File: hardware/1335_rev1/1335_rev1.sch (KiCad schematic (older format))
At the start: 12 parts, among them J1 Screw_Terminal_01x05, J2 Screw_Terminal_01x05, U1 A1335

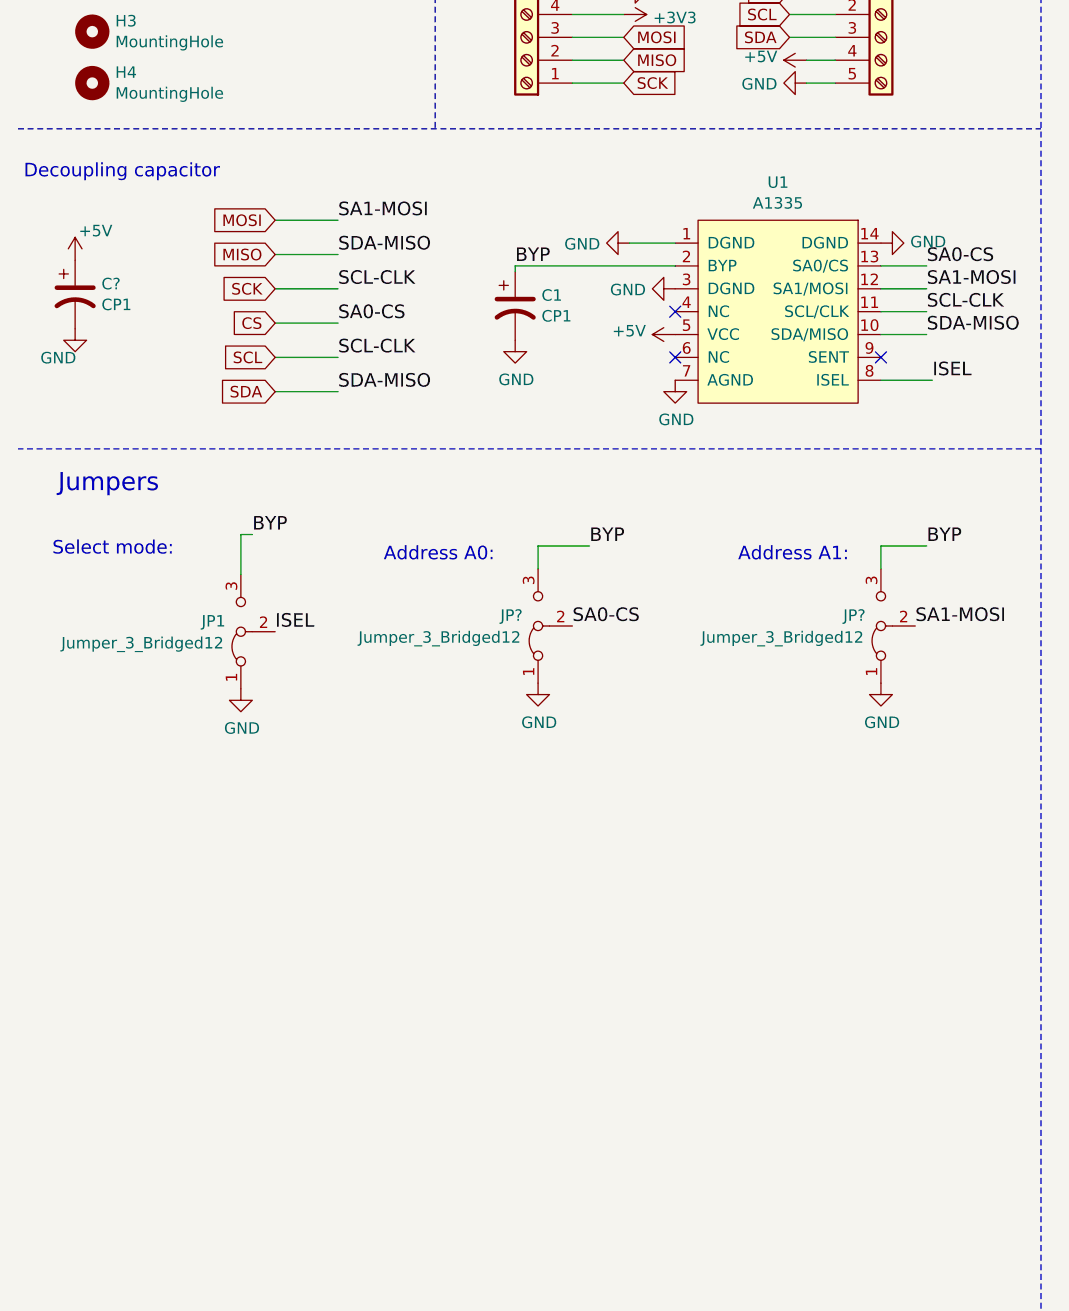
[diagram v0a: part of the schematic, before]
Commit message: Add 3d models, send to review pcb
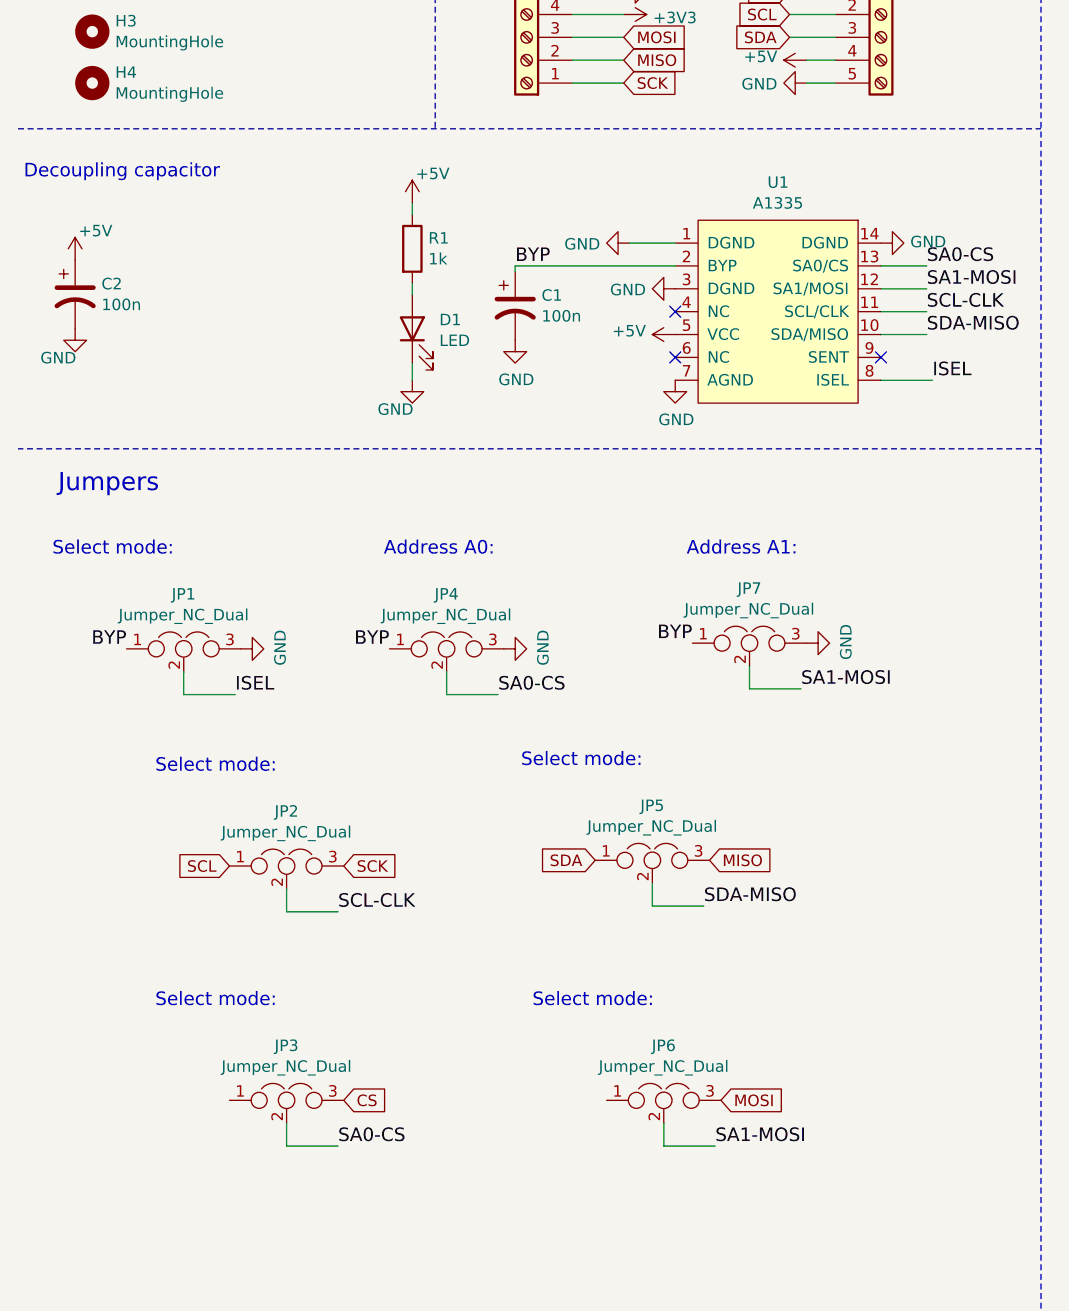
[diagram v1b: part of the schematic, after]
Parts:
- removed JP1, JP? (x2): Jumper_3_Bridged12, Jumper:SolderJumper-3_P1.3mm_Bridged2Bar12_Pad1.0x1.5mm, symbol Jumper:Jumper_3_Bridged12
- added D1: LED, LED_SMD:LED_0603_1608Metric, symbol Device:LED
- added JP1, JP2, JP3, JP4, JP5, JP6, JP7: Jumper_NC_Dual, Jumper:SolderJumper-3_P1.3mm_Open_RoundedPad1.0x1.5mm_NumberLabels, symbol Device:Jumper_NC_Dual
- added R1: 1k, Resistor_SMD:R_0603_1608Metric, symbol Device:R
- C1: value CP1 -> 100n
- C2: renamed from C?; value CP1 -> 100n
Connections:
- net +5V: now also R1.1
- net BYP: now also JP1.1, JP4.1, JP7.1
- net CS: now also JP3.3; no longer U1.13 (SA0/CS)
- net GND: now also D1.1 (K), JP1.3, JP4.3, JP7.3
- net ISEL: now also JP1.2
- net MISO: now also JP5.3; no longer J2.3 (Pin_3), U1.10 (SDA/MISO)
- net MOSI: now also JP6.3; no longer U1.12 (SA1/MOSI)
- net SCK: now also JP2.3; no longer J2.2 (Pin_2), U1.11 (SCL/CLK)
- new net: D1.2 (A), R1.2
- new net SA0-CS: JP3.2, JP4.2, U1.13 (SA0/CS)
- new net SA1-MOSI: JP6.2, JP7.2, U1.12 (SA1/MOSI)
- new net SCL: J2.2 (Pin_2), JP2.1
- new net SCL-CLK: JP2.2, U1.11 (SCL/CLK)
- new net SDA: J2.3 (Pin_3), JP5.1
- new net SDA-MISO: JP5.2, U1.10 (SDA/MISO)

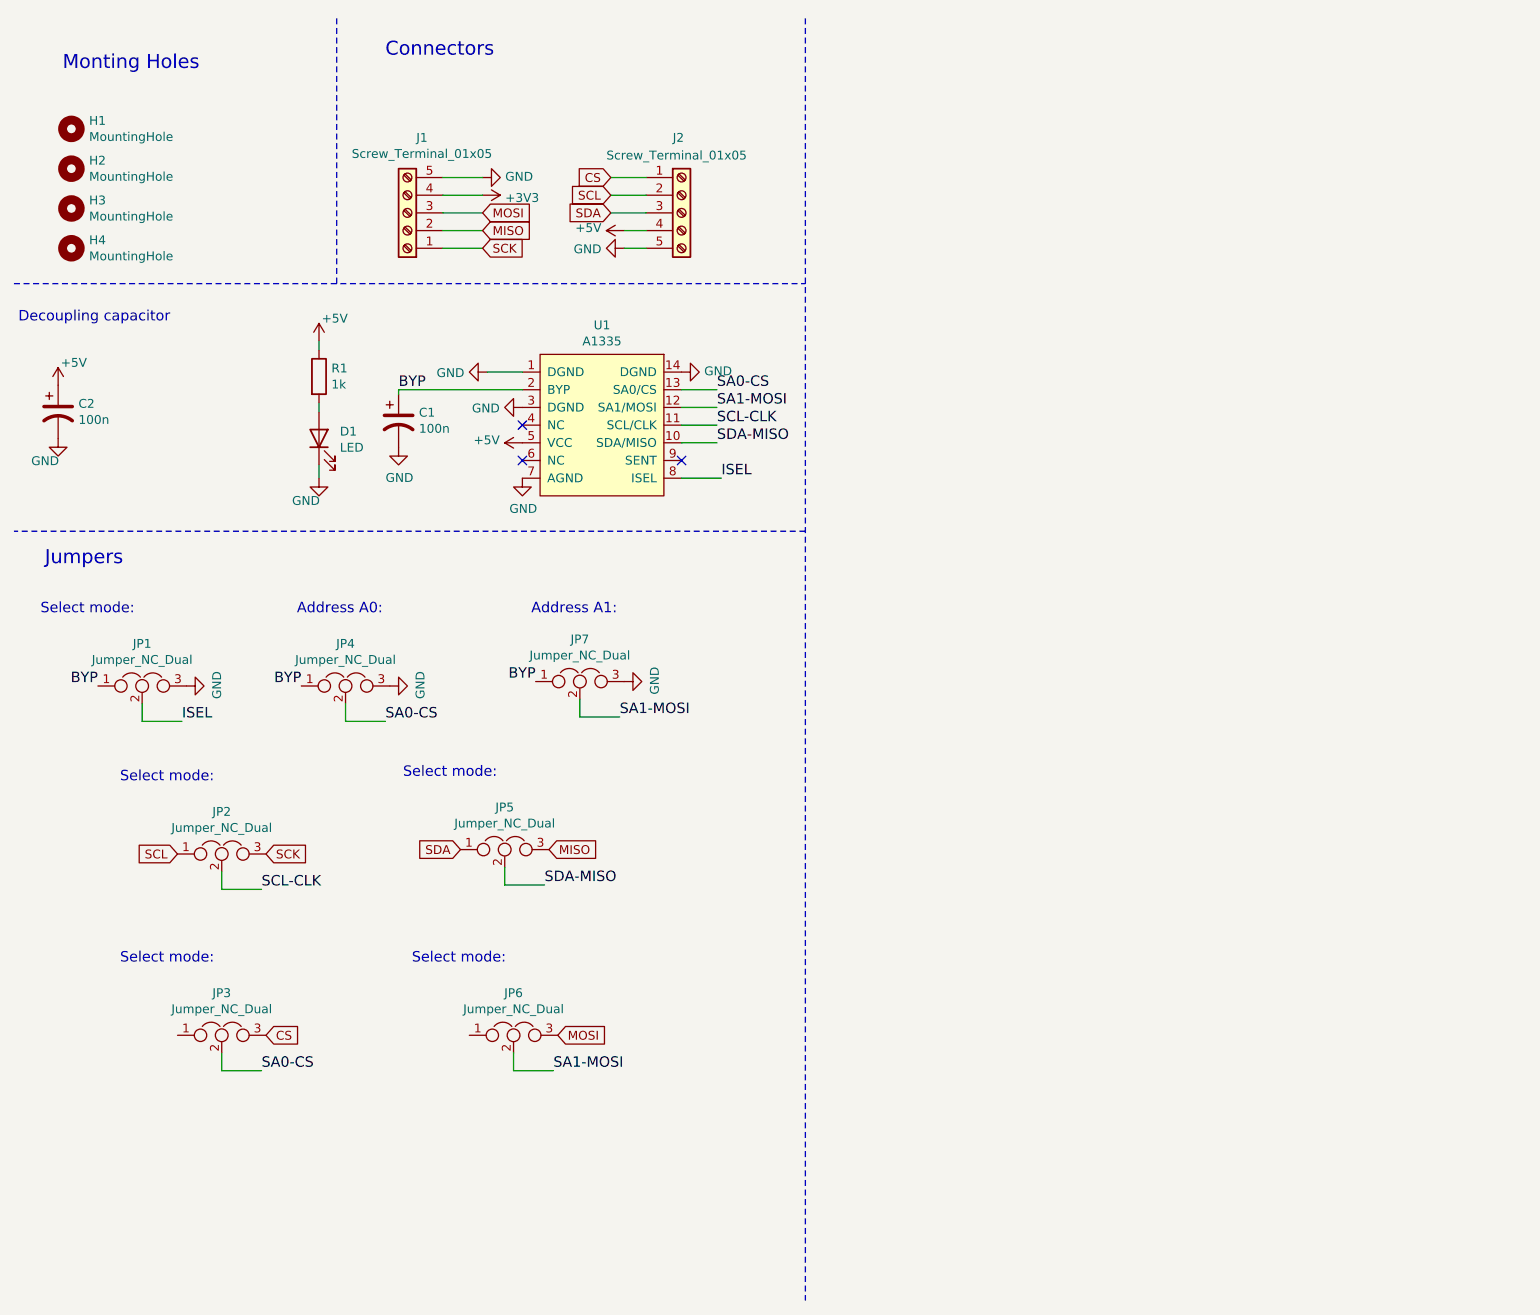
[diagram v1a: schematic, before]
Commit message: Add connectors and pull up resistors
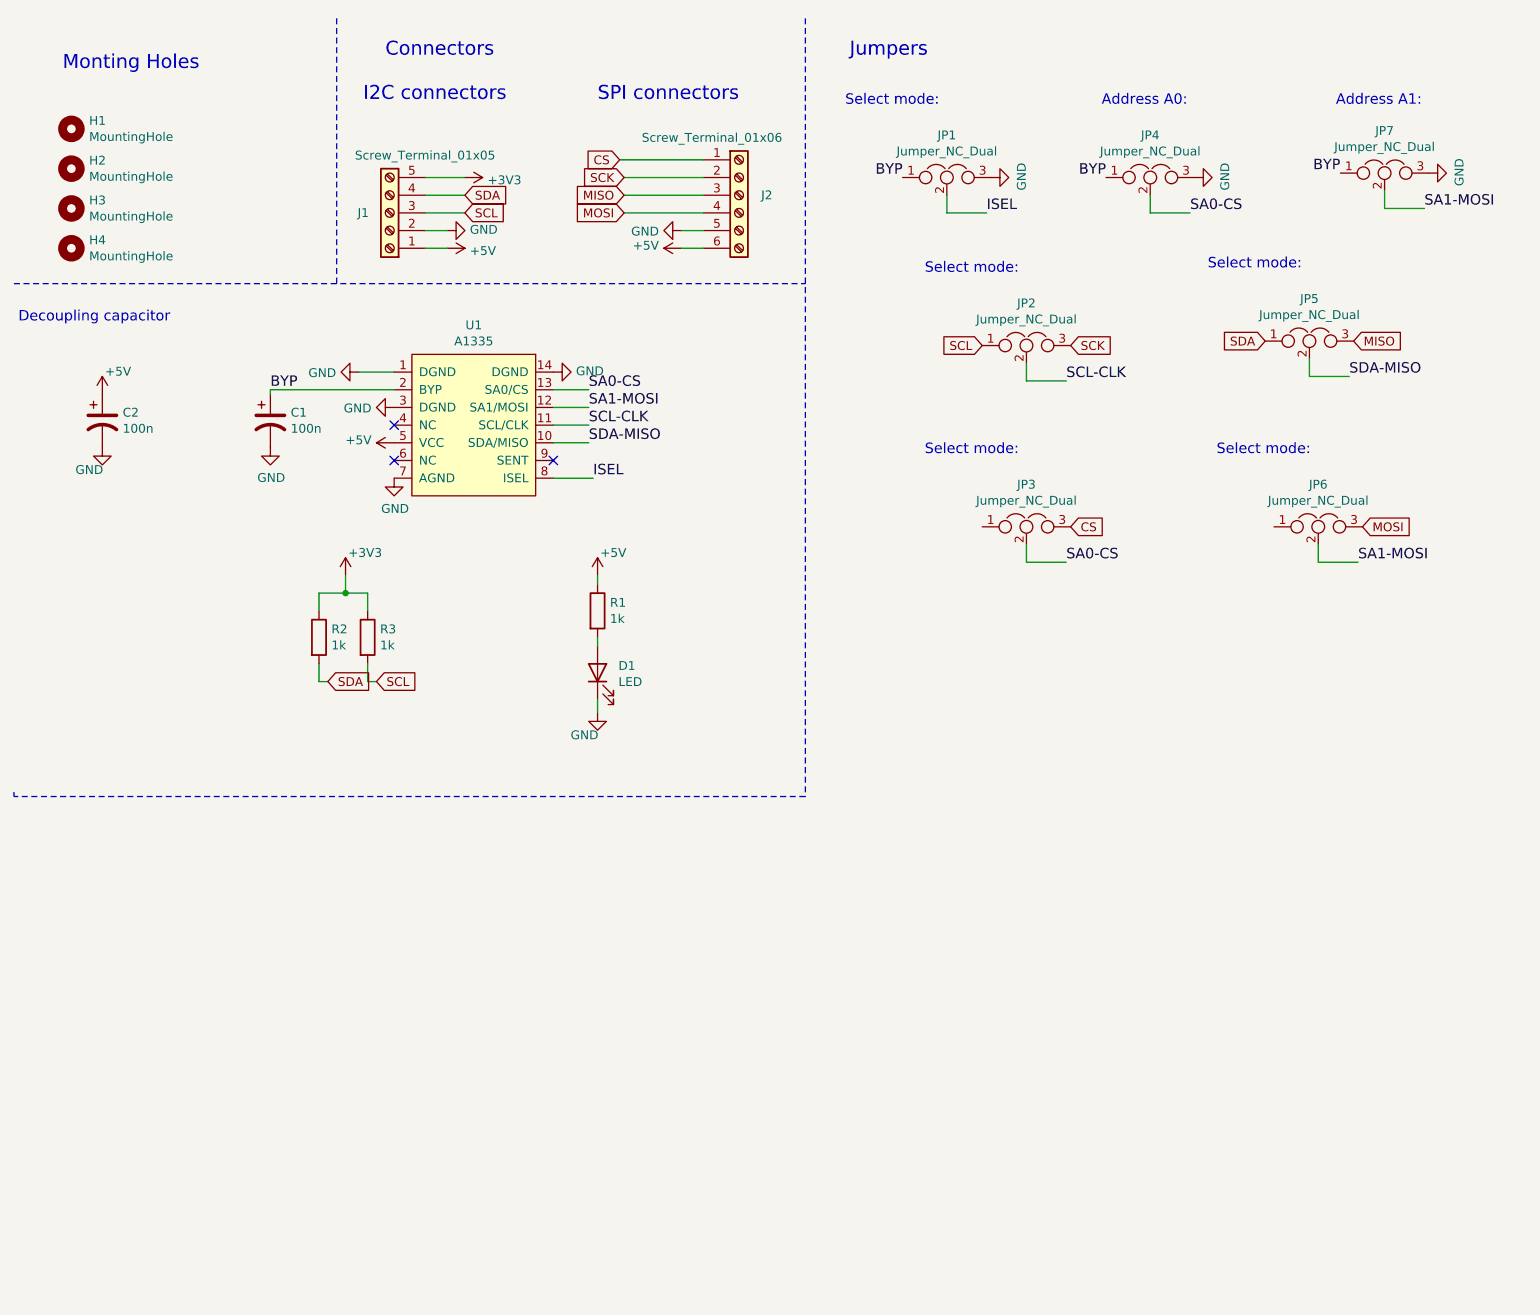
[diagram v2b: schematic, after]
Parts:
- removed J2: Screw_Terminal_01x05, Terminal_Block_WR_TBL:terminal_block_1x05_45DEG_3.81MM_5POS, symbol Connector:Screw_Terminal_01x05
- added J2: Screw_Terminal_01x06, Connector_PinHeader_2.54mm:PinHeader_1x06_P2.54mm_Horizontal, symbol Connector:Screw_Terminal_01x06
- added R2, R3: 1k, Resistor_SMD:R_0603_1608Metric, symbol Device:R
- J1: footprint Terminal_Block_WR_TBL:terminal_block_1x05_45DEG_3.81MM_5POS -> Connector_PinHeader_2.54mm:PinHeader_1x05_P2.54mm_Horizontal
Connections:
- net +3V3: now also J1.5 (Pin_5), R2.1, R3.1; no longer J1.4 (Pin_4)
- net +5V: now also J1.1 (Pin_1), J2.6 (Pin_6)
- net CS: now also J2.1 (Pin_1)
- net GND: now also J1.2 (Pin_2), J2.5 (Pin_5); no longer J1.5 (Pin_5)
- net MISO: now also J2.3 (Pin_3); no longer J1.2 (Pin_2)
- net MOSI: now also J2.4 (Pin_4); no longer J1.3 (Pin_3)
- net SCK: now also J2.2 (Pin_2); no longer J1.1 (Pin_1)
- net SCL: now also J1.3 (Pin_3), R3.2
- net SDA: now also J1.4 (Pin_4), R2.2
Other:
- note added: "I2C connectors"
- note added: "SPI connectors"
- moved on the sheet: C1, C2, D1, JP1, JP2, JP3, JP4, JP5, JP6, JP7, R1, U1

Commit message: Add F.sliks anotations
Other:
- note added: "1-2 SPI Mode\n2-3 I2C Mode"
- note added: "1-2\n2-3"
- moved on the sheet: JP2, JP3, JP5, JP6
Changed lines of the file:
@@
 Text Label 8500 1575 0    59   ~ 0
 SA1-MOSI
-Text Notes 5675 1950 0    59   ~ 0
+Text Notes 5650 2325 0    59   ~ 0
 Select mode:\n
 $Comp
 L Device:Jumper_NC_Dual JP2
 U 1 1 604B71D7
-P 6250 2350
-F 0 "JP2" H 6250 2589 50  0000 C CNN
-F 1 "Jumper_NC_Dual" H 6250 2498 50  0000 C CNN
-F 2 "Jumper:SolderJumper-3_P1.3mm_Open_RoundedPad1.0x1.5mm_NumberLabels" H 6250 2350 50  0001 C CNN
-F 3 "~" H 6250 2350 50  0001 C CNN
-	1    6250 2350
-	1    0    0    -1
-$EndComp
-Wire Wire Line
-	6250 2450 6250 2550
-Wire Wire Line
-	6250 2550 6475 2550
-Text Notes 7275 1925 0    59   ~ 0
+P 6225 2725
+F 0 "JP2" H 6225 2964 50  0000 C CNN
+F 1 "Jumper_NC_Dual" H 6225 2873 50  0000 C CNN
+F 2 "Jumper:SolderJumper-3_P1.3mm_Open_RoundedPad1.0x1.5mm_NumberLabels" H 6225 2725 50  0001 C CNN
+F 3 "~" H 6225 2725 50  0001 C CNN
+	1    6225 2725
+	1    0    0    -1
+$EndComp
+Wire Wire Line
+	6225 2825 6225 2925
+Wire Wire Line
+	6225 2925 6450 2925
+Text Notes 7250 2300 0    59   ~ 0
 Select mode:\n
 $Comp
 L Device:Jumper_NC_Dual JP5
 U 1 1 604B9F66
-P 7850 2325
-F 0 "JP5" H 7850 2564 50  0000 C CNN
-F 1 "Jumper_NC_Dual" H 7850 2473 50  0000 C CNN
-F 2 "Jumper:SolderJumper-3_P1.3mm_Open_RoundedPad1.0x1.5mm_NumberLabels" H 7850 2325 50  0001 C CNN
-F 3 "~" H 7850 2325 50  0001 C CNN
-	1    7850 2325
-	1    0    0    -1
-$EndComp
-Wire Wire Line
-	7850 2425 7850 2525
-Wire Wire Line
-	7850 2525 8075 2525
-Text Notes 5675 2975 0    59   ~ 0
+P 7825 2700
+F 0 "JP5" H 7825 2939 50  0000 C CNN
+F 1 "Jumper_NC_Dual" H 7825 2848 50  0000 C CNN
+F 2 "Jumper:SolderJumper-3_P1.3mm_Open_RoundedPad1.0x1.5mm_NumberLabels" H 7825 2700 50  0001 C CNN
+F 3 "~" H 7825 2700 50  0001 C CNN
+	1    7825 2700
+	1    0    0    -1
+$EndComp
+Wire Wire Line
+	7825 2800 7825 2900
+Wire Wire Line
+	7825 2900 8050 2900
+Text Notes 5650 3350 0    59   ~ 0
 Select mode:\n
 $Comp
 L Device:Jumper_NC_Dual JP3
 U 1 1 604BBF53
-P 6250 3375
-F 0 "JP3" H 6250 3614 50  0000 C CNN
-F 1 "Jumper_NC_Dual" H 6250 3523 50  0000 C CNN
-F 2 "Jumper:SolderJumper-3_P1.3mm_Open_RoundedPad1.0x1.5mm_NumberLabels" H 6250 3375 50  0001 C CNN
-F 3 "~" H 6250 3375 50  0001 C CNN
-	1    6250 3375
-	1    0    0    -1
-$EndComp
-Wire Wire Line
-	6250 3475 6250 3575
-Wire Wire Line
-	6250 3575 6475 3575
-Text Notes 7325 2975 0    59   ~ 0
+P 6225 3750
+F 0 "JP3" H 6225 3989 50  0000 C CNN
+F 1 "Jumper_NC_Dual" H 6225 3898 50  0000 C CNN
+F 2 "Jumper:SolderJumper-3_P1.3mm_Open_RoundedPad1.0x1.5mm_NumberLabels" H 6225 3750 50  0001 C CNN
+F 3 "~" H 6225 3750 50  0001 C CNN
+	1    6225 3750
+	1    0    0    -1
+$EndComp
+Wire Wire Line
+	6225 3850 6225 3950
+Wire Wire Line
+	6225 3950 6450 3950
+Text Notes 7300 3350 0    59   ~ 0
 Select mode:\n
 $Comp
 L Device:Jumper_NC_Dual JP6
 U 1 1 604BD230
-P 7900 3375
-F 0 "JP6" H 7900 3614 50  0000 C CNN
-F 1 "Jumper_NC_Dual" H 7900 3523 50  0000 C CNN
-F 2 "Jumper:SolderJumper-3_P1.3mm_Open_RoundedPad1.0x1.5mm_NumberLabels" H 7900 3375 50  0001 C CNN
-F 3 "~" H 7900 3375 50  0001 C CNN
-	1    7900 3375
-	1    0    0    -1
-$EndComp
-Wire Wire Line
-	7900 3475 7900 3575
-Wire Wire Line
-	7900 3575 8125 3575
-Text Label 6475 2550 0    59   ~ 0
+P 7875 3750
+F 0 "JP6" H 7875 3989 50  0000 C CNN
+F 1 "Jumper_NC_Dual" H 7875 3898 50  0000 C CNN
+F 2 "Jumper:SolderJumper-3_P1.3mm_Open_RoundedPad1.0x1.5mm_NumberLabels" H 7875 3750 50  0001 C CNN
+F 3 "~" H 7875 3750 50  0001 C CNN
+	1    7875 3750
+	1    0    0    -1
+$EndComp
+Wire Wire Line
+	7875 3850 7875 3950
+Wire Wire Line
+	7875 3950 8100 3950
+Text Label 6450 2925 0    59   ~ 0
 SCL-CLK
-Text GLabel 6000 2350 0    50   Input ~ 0
+Text GLabel 5975 2725 0    50   Input ~ 0
 SCL
-Text GLabel 6500 2350 2    50   Input ~ 0
+Text GLabel 6475 2725 2    50   Input ~ 0
 SCK
-Text Label 8075 2525 0    59   ~ 0
+Text Label 8050 2900 0    59   ~ 0
 SDA-MISO
-Text GLabel 7600 2325 0    50   Input ~ 0
+Text GLabel 7575 2700 0    50   Input ~ 0
 SDA
-Text GLabel 8100 2325 2    50   Input ~ 0
+Text GLabel 8075 2700 2    50   Input ~ 0
 MISO
-Text Label 6475 3575 0    59   ~ 0
+Text Label 6450 3950 0    59   ~ 0
 SA0-CS
-Text GLabel 6500 3375 2    50   Input ~ 0
+Text GLabel 6475 3750 2    50   Input ~ 0
 CS
-Text Label 8125 3575 0    59   ~ 0
+Text Label 8100 3950 0    59   ~ 0
 SA1-MOSI
-Text GLabel 8150 3375 2    50   Input ~ 0
+Text GLabel 8125 3750 2    50   Input ~ 0
 MOSI
 $Comp
@@
 Wire Notes Line
 	5000 500  5000 4900
+Text Notes 5300 1800 0    59   ~ 0
+1-2 SPI Mode\n2-3 I2C Mode
+Text Notes 6675 1825 0    59   ~ 0
+1-2\n2-3
 $EndSCHEMATC
